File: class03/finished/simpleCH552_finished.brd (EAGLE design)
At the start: 40.6 x 12 mm, 12 parts, among them U1 CH552G, X1 USBPCB

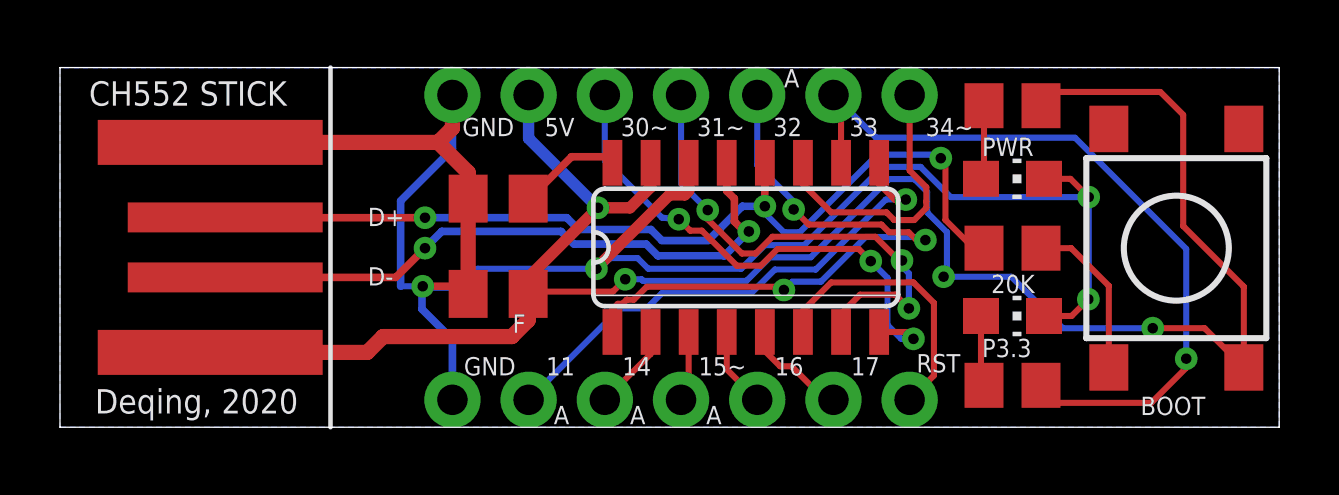
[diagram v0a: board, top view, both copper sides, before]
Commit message: update to USB shell model
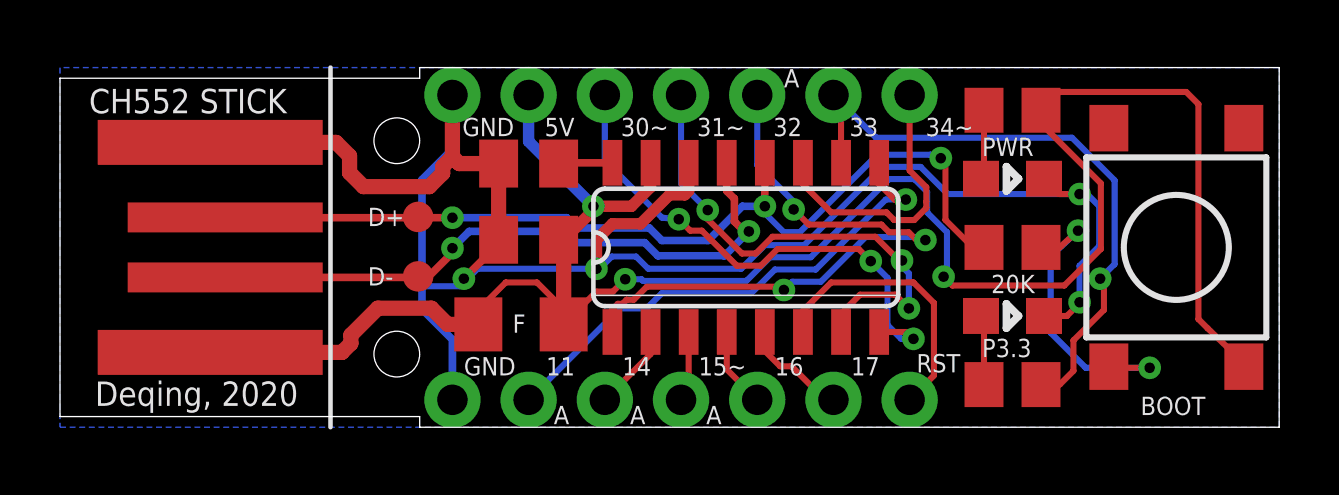
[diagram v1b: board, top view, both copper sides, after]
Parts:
- added F1: (no value), adafruit:R1206
- added TP1, TP2: TEST-POINT3X4, SparkFun-Connectors:PAD.03X.04
- LED1: value RED -> PWR; device led:CHIP-LED0805 -> BeagleBone_Black_Wireless:GHI-BASICCOMPONENTS_0805-LED
- LED2: value GREEN -> P3.3; device led:CHIP-LED0805 -> BeagleBone_Black_Wireless:GHI-BASICCOMPONENTS_0805-LED
- moved C1 2.07 mm to (15.6, 6.25)
- moved C2 1.55 mm to (15.6, 8.79)
- moved R2 0.15 mm to (31.8, 10.6)
- turned LED1 to 90 degrees
- turned LED2 to 90 degrees
- renumbered U1 to U2
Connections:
- net +5V: now also F1.1, F1.2
- net GND: now also LED1.K, LED2.K; no longer LED1.C, LED2.C
- net USB_D+: now also TP2.P$1
- net USB_D-: now also TP1.P$1
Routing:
- net N$1: track 5.50 -> 10.4 mm, vias 0 -> 2
- net P3.3: track 25.8 -> 21.2 mm
- net +5V: track 67.3 -> 70.2 mm, vias 4 -> 3
- net 3.3V: track 3.46 -> 1.80 mm
- net USB_D+: track 31.5 -> 32.6 mm
- net GND: track 65.1 -> 65.6 mm
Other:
- outline, holes or cut-outs redrawn
- board text added: "Deqing Sun, 2020 Try Ch55xduino with this board"
- board text added: "Deqing Sun, 2022 Prototyping Electronic Devices"
- board text removed: "Deqing Sun, 2020 Prototyping Electronic Devices"
